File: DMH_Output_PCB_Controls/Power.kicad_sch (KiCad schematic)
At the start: 68 parts, among them J0 Conn_01x01, J100 IDC_02x05, U1 TL072, U10 NE5532, U11 TL074, U12 NE5532, U13 NE5532, U14 NE5532, U15 NE5532, U16 NE5532, U17 NE5532, U18 NE5532, U19 NE5532, U2 LM339, U20 TL072, U24 LM339, U25 LM339, U3 LM339, U4 LM339, U5 LM339, U6 LM339, U7 TL072, U8 TL074, U9 NE5532

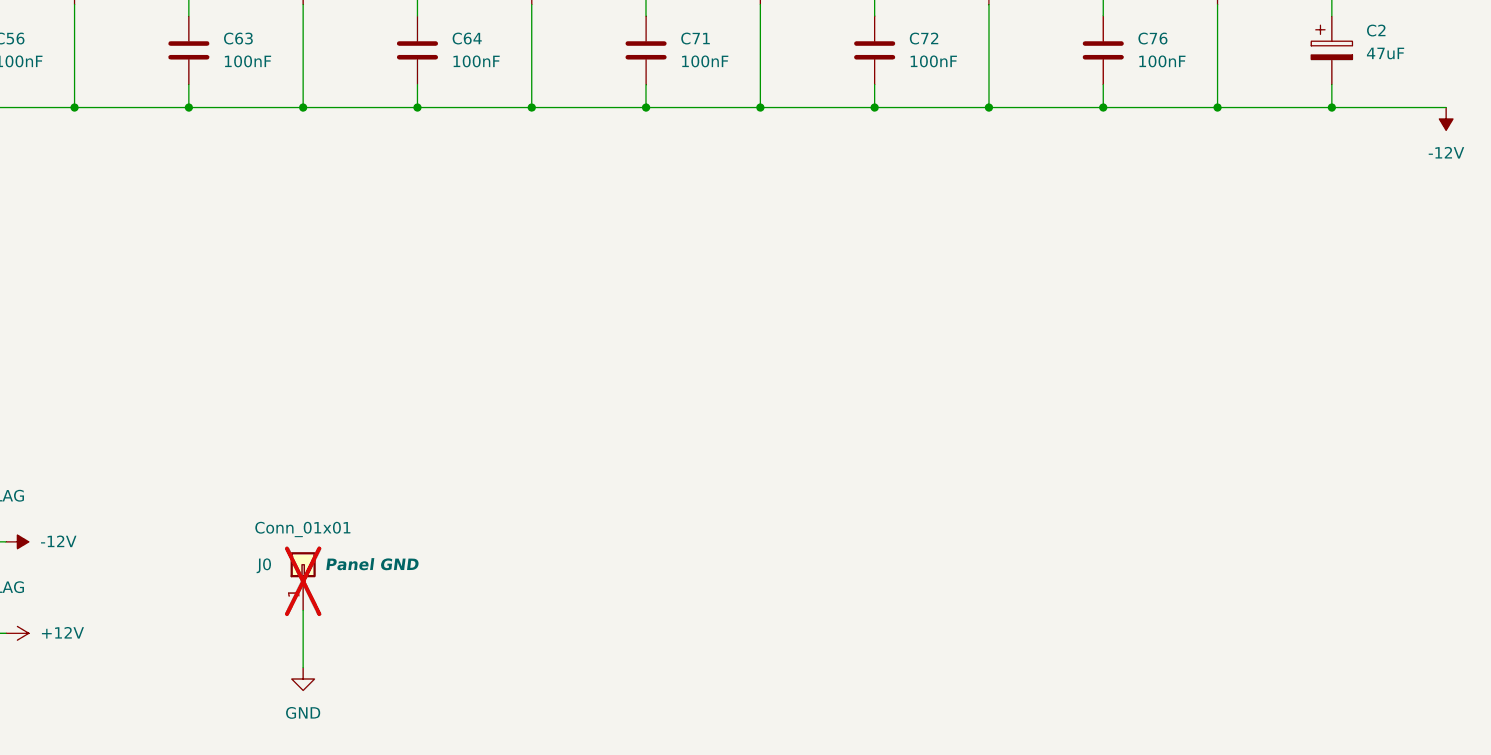
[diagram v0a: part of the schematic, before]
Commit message: Adjusted meter circuits
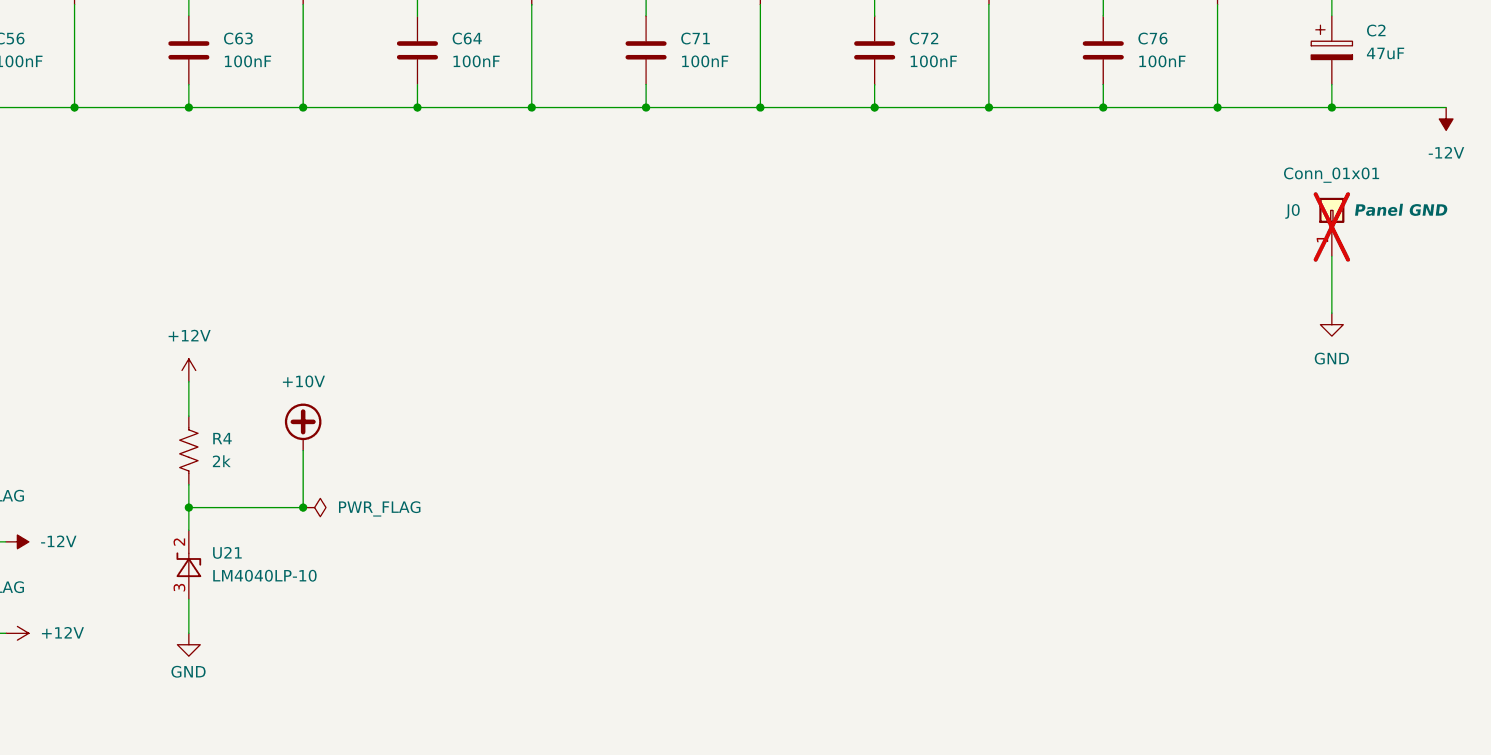
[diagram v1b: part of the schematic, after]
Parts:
- added R4: 2k, Resistor_THT:R_Axial_DIN0207_L6.3mm_D2.5mm_P7.62mm_Horizontal, symbol Device:R_US
- added U21: LM4040LP-10, Package_TO_SOT_THT:TO-92_Inline, symbol Reference_Voltage:LM4040LP-10
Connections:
- net +12V: now also R4.2
- net GND: now also U21.3 (A)
- new net +10V: R4.1, U21.2 (K)
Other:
- moved on the sheet: J0

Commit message: Starting Controls PCB design
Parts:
- added J10: Conn_01x06, Connector_PinSocket_2.54mm:PinSocket_1x06_P2.54mm_Vertical, symbol Connector_Generic:Conn_01x06
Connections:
- net +10V: now also J10.2 (Pin_2)
- net +12V: now also J10.1 (Pin_1)
- net -12V: now also J10.6 (Pin_6)
- net GND: now also J10.3 (Pin_3), J10.4 (Pin_4), J10.5 (Pin_5)

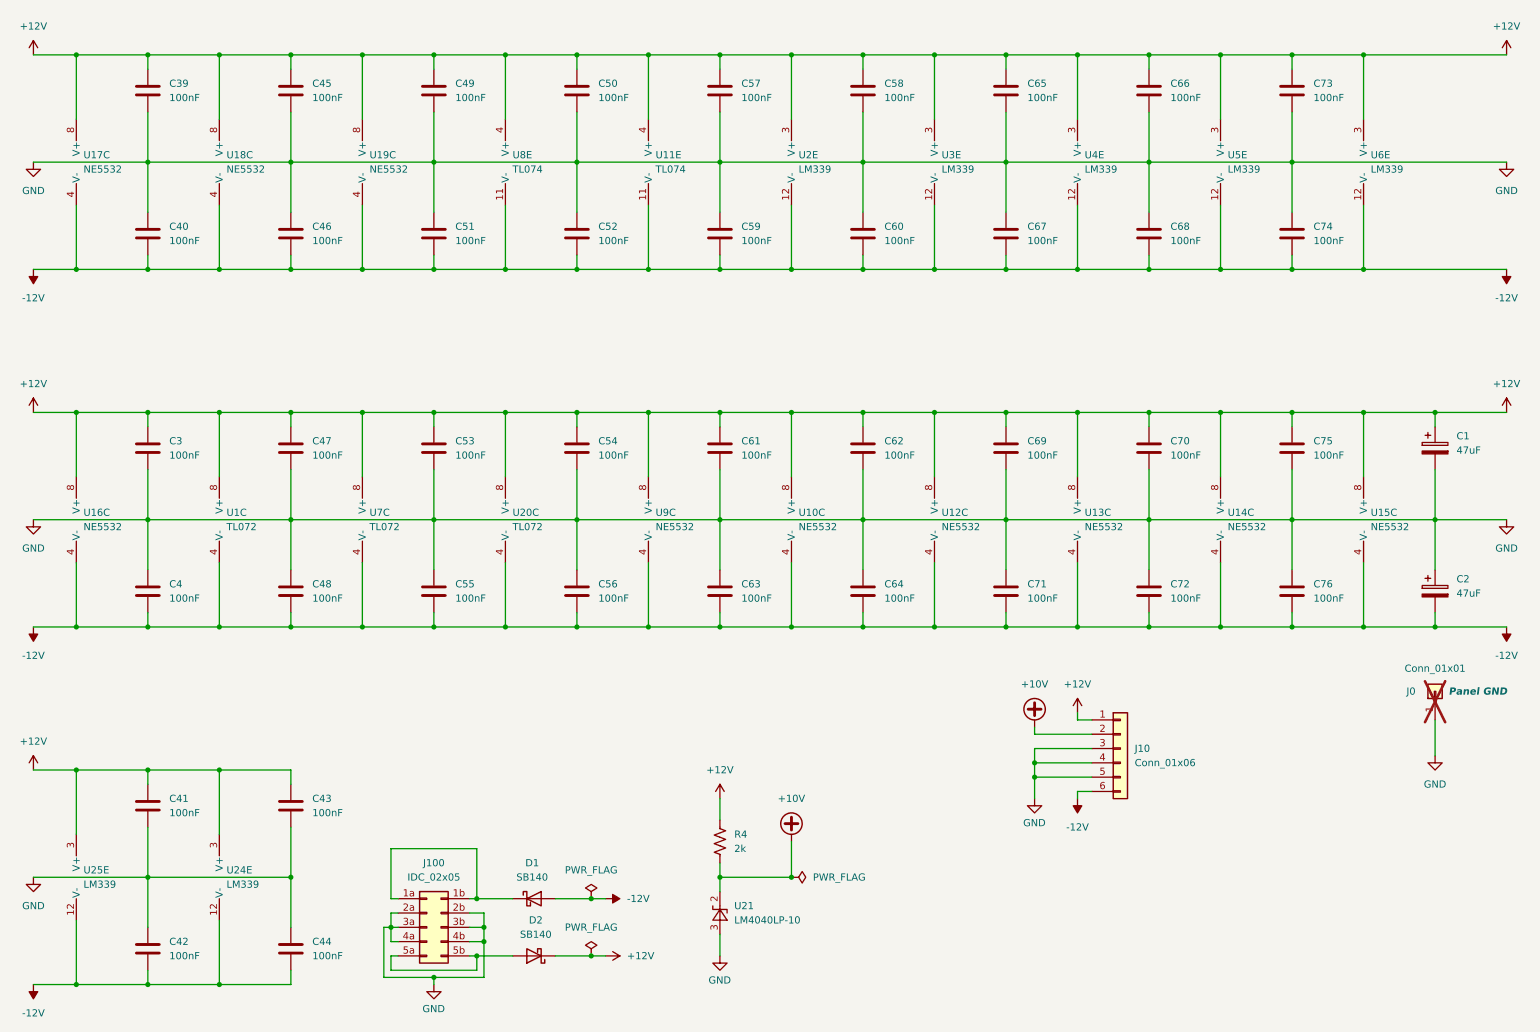
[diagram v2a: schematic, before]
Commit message: Controls PCB placement ongoing
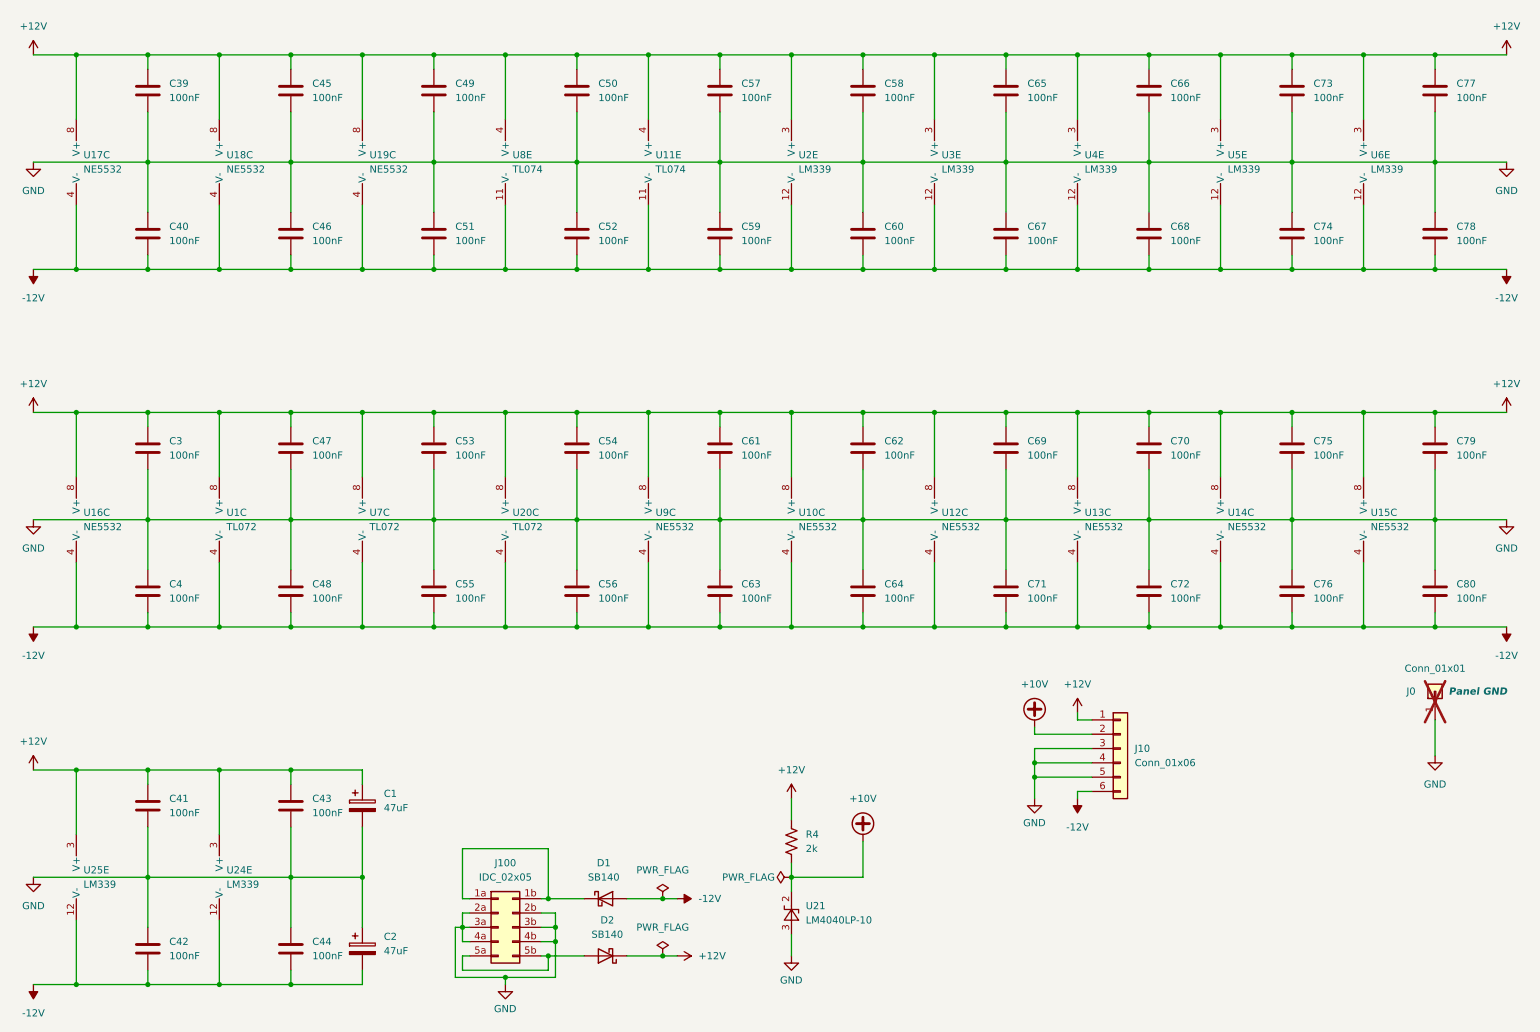
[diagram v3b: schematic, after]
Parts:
- added C77, C78, C79, C80: 100nF, Capacitor_THT:C_Disc_D4.3mm_W1.9mm_P5.00mm, symbol Device:C
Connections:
- net +12V: now also C77.1, C79.1
- net -12V: now also C78.2, C80.2
- net GND: now also C77.2, C78.1, C79.2, C80.1
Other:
- moved on the sheet: C1, C2, D1, D2, J100, R4, U21

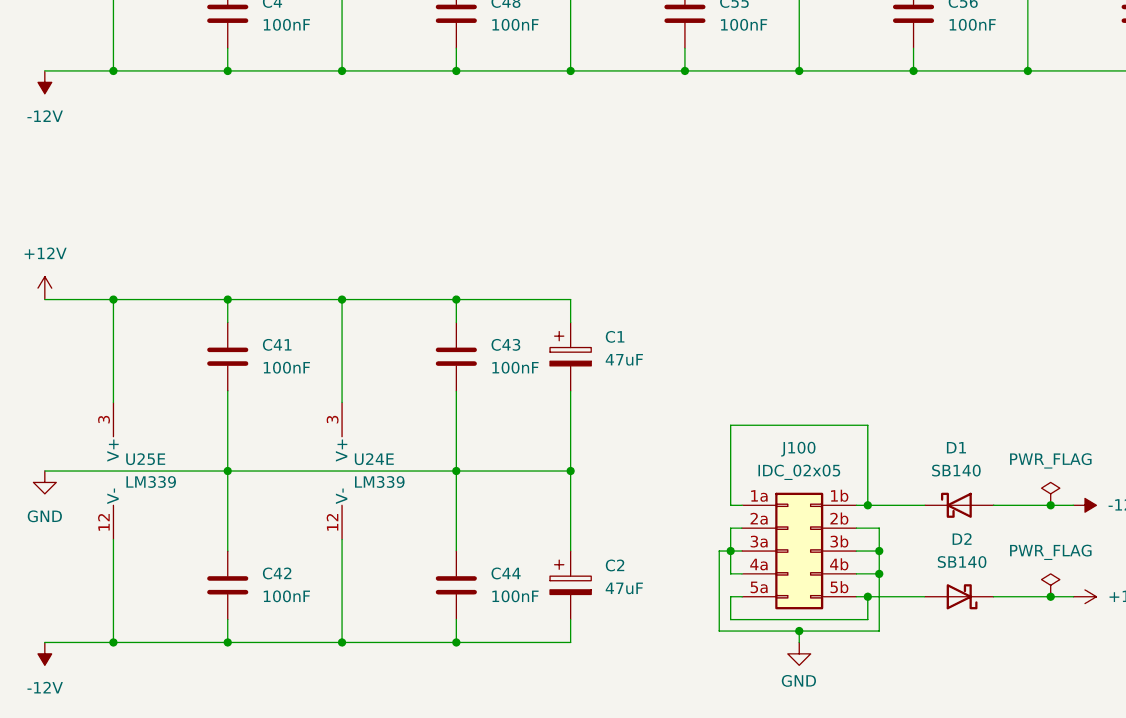
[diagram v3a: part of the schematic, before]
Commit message: Controls PCB placement in progress
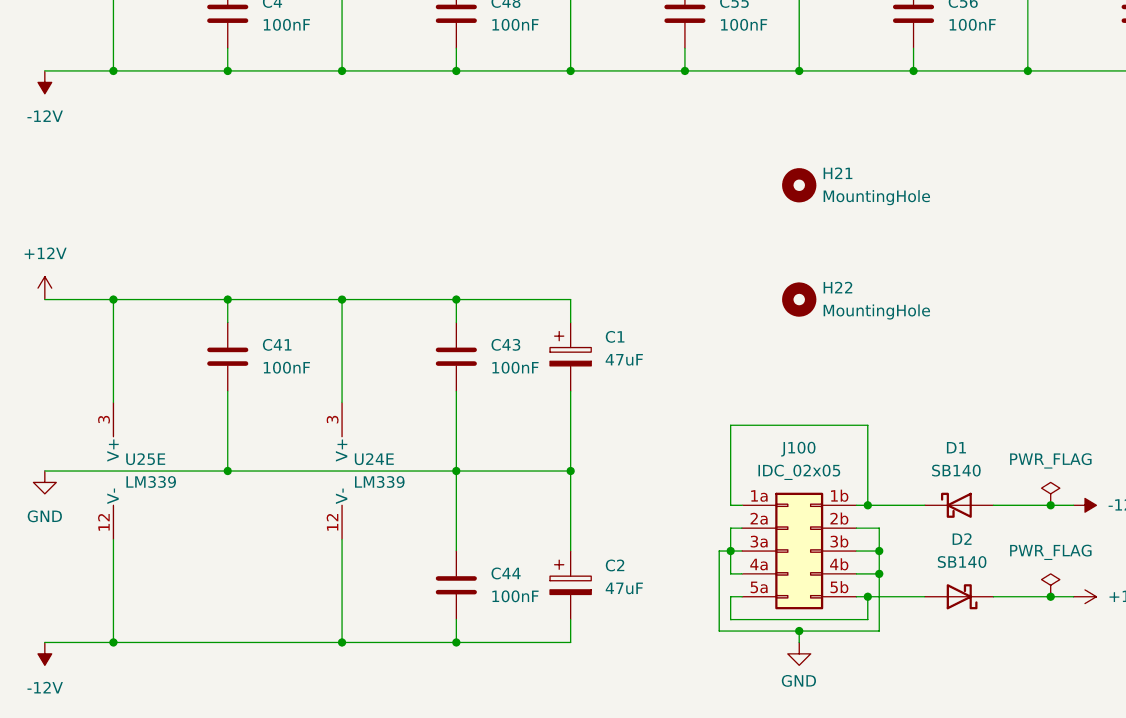
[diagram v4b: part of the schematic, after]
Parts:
- removed C42: 100nF, Capacitor_THT:C_Disc_D4.3mm_W1.9mm_P5.00mm, symbol Device:C
- added H21, H22: MountingHole, MountingHole:MountingHole_2.2mm_M2, symbol Mechanical:MountingHole
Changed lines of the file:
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@@
 	)
 	(junction
-		(at 38.1 190.5)
-		(diameter 0)
-		(color 0 0 0 0)
-	)
-	(junction
 		(at 241.3 107.95)
 		(diameter 0)
@@
 	(wire
 		(pts
-			(xy 38.1 190.5) (xy 50.8 190.5)
+			(xy 25.4 190.5) (xy 50.8 190.5)
 		)
 		(stroke
@@
 	(wire
 		(pts
-			(xy 38.1 171.45) (xy 38.1 180.34)
-		)
-		(stroke
-			(width 0)
-			(type default)
-		)
-	)
-	(wire
-		(pts
 			(xy 63.5 107.95) (xy 88.9 107.95)
 		)
@@
 	(wire
 		(pts
-			(xy 25.4 190.5) (xy 38.1 190.5)
-		)
-		(stroke
-			(width 0)
-			(type default)
-		)
-	)
-	(wire
-		(pts
 			(xy 114.3 63.5) (xy 127 63.5)
 		)
@@
 	(wire
 		(pts
-			(xy 38.1 187.96) (xy 38.1 190.5)
-		)
-		(stroke
-			(width 0)
-			(type default)
-		)
-	)
-	(wire
-		(pts
 			(xy 114.3 60.96) (xy 114.3 63.5)
 		)
@@
 	)
 	(symbol
+		(lib_id "Mechanical:MountingHole")
+		(at 101.6 139.7 0)
+		(unit 1)
+		(exclude_from_sim no)
+		(in_bom no)
+		(on_board yes)
+		(dnp no)
+		(fields_autoplaced yes)
+		(property "Reference" "H21"
+			(at 104.14 138.4299 0)
+			(effects
+				(font
+					(size 1.27 1.27)
+				)
+				(justify left)
+			)
+		)
+		(property "Value" "MountingHole"
+			(at 104.14 140.9699 0)
+			(effects
+				(font
+					(size 1.27 1.27)
+				)
+				(justify left)
+			)
+		)
+		(property "Footprint" "MountingHole:MountingHole_2.2mm_M2"
+			(at 101.6 139.7 0)
+			(effects
+				(font
+					(size 1.27 1.27)
+				)
+				(hide yes)
+			)
+		)
+		(property "Datasheet" "~"
+			(at 101.6 139.7 0)
+			(effects
+				(font
+					(size 1.27 1.27)
+				)
+				(hide yes)
+			)
+		)
+		(property "Description" "Mounting Hole without connection"
+			(at 101.6 139.7 0)
+			(effects
+				(font
+					(size 1.27 1.27)
+				)
+				(hide yes)
+			)
+		)
+		(instances
+			(project ""
+				(path "/58f4306d-5387-4983-bb08-41a2313fd315/0cdf34b2-39cd-4d9e-981a-97cd34791509"
+					(reference "H21")
+					(unit 1)
+				)
+			)
+		)
+	)
+	(symbol
 		(lib_id "power:GND")
 		(at 152.4 185.42 0)
@@
 	)
 	(symbol
+		(lib_id "Mechanical:MountingHole")
+		(at 101.6 152.4 0)
+		(unit 1)
+		(exclude_from_sim no)
+		(in_bom no)
+		(on_board yes)
+		(dnp no)
+		(fields_autoplaced yes)
+		(property "Reference" "H22"
+			(at 104.14 151.1299 0)
+			(effects
+				(font
+					(size 1.27 1.27)
+				)
+				(justify left)
+			)
+		)
+		(property "Value" "MountingHole"
+			(at 104.14 153.6699 0)
+			(effects
+				(font
+					(size 1.27 1.27)
+				)
+				(justify left)
+			)
+		)
+		(property "Footprint" "MountingHole:MountingHole_2.2mm_M2"
+			(at 101.6 152.4 0)
+			(effects
+				(font
+					(size 1.27 1.27)
+				)
+				(hide yes)
+			)
+		)
+		(property "Datasheet" "~"
+			(at 101.6 152.4 0)
+			(effects
+				(font
+					(size 1.27 1.27)
+				)
+				(hide yes)
+			)
+		)
+		(property "Description" "Mounting Hole without connection"
+			(at 101.6 152.4 0)
+			(effects
+				(font
+					(size 1.27 1.27)
+				)
+				(hide yes)
+			)
+		)
+		(instances
+			(project "DMH_Output_PCB_Controls"
+				(path "/58f4306d-5387-4983-bb08-41a2313fd315/0cdf34b2-39cd-4d9e-981a-97cd34791509"
+					(reference "H22")
+					(unit 1)
+				)
+			)
+		)
+	)
+	(symbol
 		(lib_id "Device:C")
 		(at 139.7 57.15 0)
@@
 					(unit 1)
 				)
-			)
-		)
-	)
-	(symbol
-		(lib_id "Device:C")
-		(at 38.1 184.15 0)
-		(unit 1)
-		(exclude_from_sim no)
-		(in_bom yes)
-		(on_board yes)
-		(dnp no)
-		(fields_autoplaced yes)
-		(property "Reference" "C42"
-			(at 41.91 182.8799 0)
-			(effects
-				(font
-					(size 1.27 1.27)
-				)
-				(justify left)
-			)
-		)
-		(property "Value" "100nF"
-			(at 41.91 185.4199 0)
-			(effects
-				(font
-					(size 1.27 1.27)
-				)
-				(justify left)
-			)
-		)
-		(property "Footprint" "Capacitor_THT:C_Disc_D4.3mm_W1.9mm_P5.00mm"
-			(at 39.0652 187.96 0)
-			(effects
-				(font
-					(size 1.27 1.27)
-				)
-				(hide yes)
-			)
-		)
-		(property "Datasheet" "~"
-			(at 38.1 184.15 0)
-			(effects
-				(font
-					(size 1.27 1.27)
-				)
-				(hide yes)
-			)
-		)
-		(property "Description" "Unpolarized capacitor"
-			(at 38.1 184.15 0)
-			(effects
-				(font
-					(size 1.27 1.27)
-				)
-				(hide yes)
-			)
-		)
-		(pin "2"
-		)
-		(pin "1"
-		)
-		(instances
-			(project "DMH_Output_PCB_1"
-				(path "/58f4306d-5387-4983-bb08-41a2313fd315/0cdf34b2-39cd-4d9e-981a-97cd34791509"
-					(reference "C42")
-					(unit 1)
-				)
